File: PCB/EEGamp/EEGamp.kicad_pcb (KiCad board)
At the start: 2 copper layers, 92.4 x 113.1 mm, 100 parts, among them J1 Conn_02x17, Q1 BC847, Q2 BC847, Q3 BC847, Q4 BC847, Q5 BC857, Q6 BC857, Q7 BC857, Q8 BC857, U1 TLC277, U2 AD620, U3 AD620, U4 TLC277, U5 TLC277, U6 TLC277

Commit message: Test points added
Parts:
- added TP1: CH2, TestPoint:TestPoint_2Pads_Pitch2.54mm_Drill0.8mm, F.Cu at (143.7, 127.5)
- added TP2: CH1, TestPoint:TestPoint_2Pads_Pitch2.54mm_Drill0.8mm, F.Cu at (144.3, 100.5)
- added TP3: R_LEG, TestPoint:TestPoint_Loop_D1.80mm_Drill1.0mm_Beaded, F.Cu at (144.1, 87.5)
- added TP4: DC Check CH2, TestPoint:TestPoint_Loop_D1.80mm_Drill1.0mm_Beaded, F.Cu at (90.6, 112.3)
- added TP5: DC Check CH1, TestPoint:TestPoint_Loop_D1.80mm_Drill1.0mm_Beaded, F.Cu at (98.1, 89.4)
- added TP6: CalGND, TestPoint:TestPoint_Loop_D1.80mm_Drill1.0mm_Beaded, F.Cu at (148.2, 39.7)
- added TP7: CalU, TestPoint:TestPoint_Loop_D1.80mm_Drill1.0mm_Beaded, F.Cu at (139.0, 41.7)
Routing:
- net /R_LEG: track 10.2 -> 30.4 mm, vias 0 -> 1
- net Net-(C15-Pad2): track 7.11 -> 23.2 mm, vias 0 -> 1
- net /CH2+: track 0.00 -> 10.8 mm
- net /CH2-: track 0.00 -> 10.6 mm
- net /CH1-: track 0.00 -> 10.6 mm
- net /CH1+: track 0.00 -> 10.5 mm
- net Net-(R32-Pad2): track 0.00 -> 5.15 mm
- net Net-(R33-Pad2): track 0.00 -> 4.97 mm

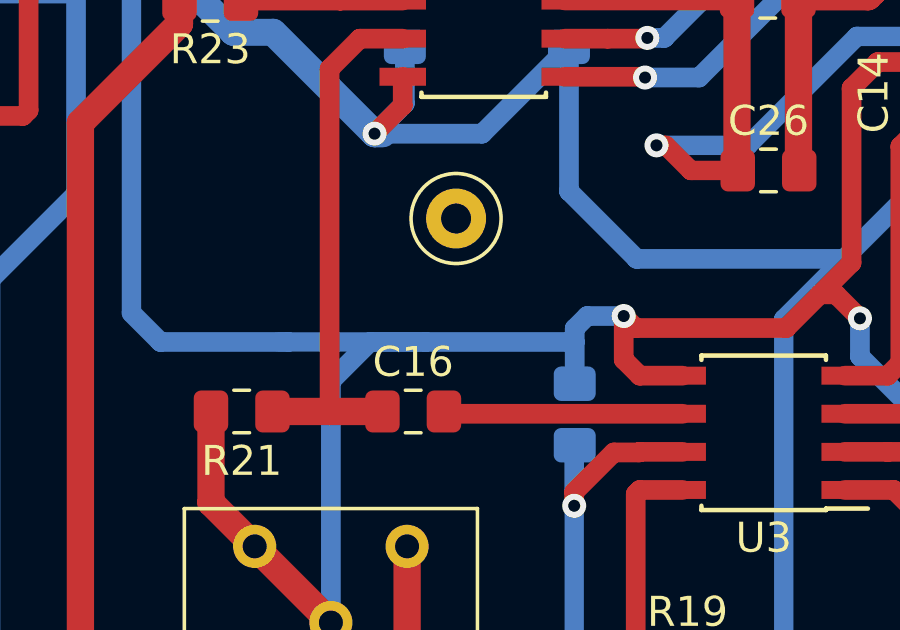
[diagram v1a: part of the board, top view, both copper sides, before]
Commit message: Fixed unrouted track
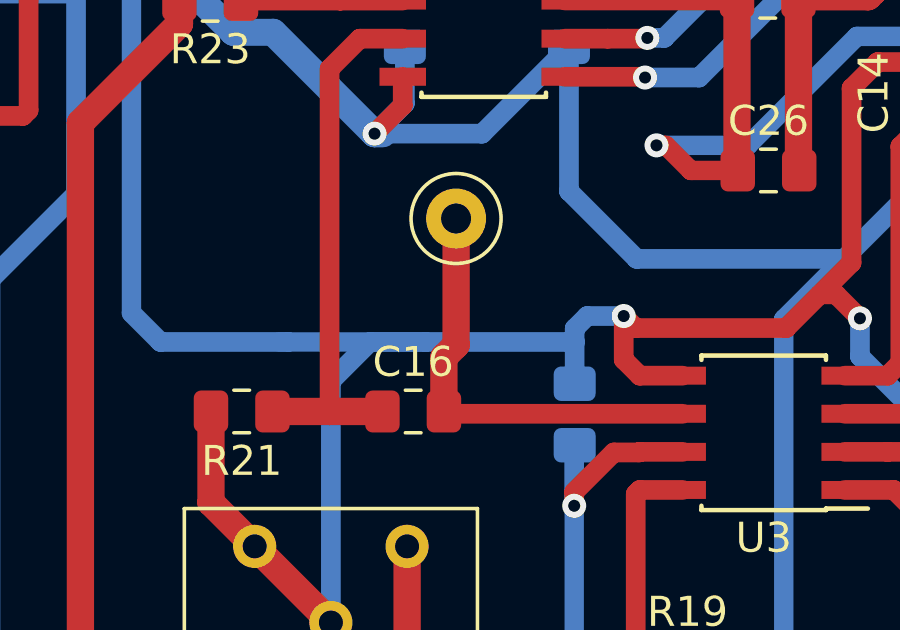
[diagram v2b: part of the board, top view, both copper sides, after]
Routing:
- net Net-(C16-Pad2): track 7.99 -> 14.6 mm
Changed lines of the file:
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@@
     (thickness 1.6)
     (drawings 8)
-    (tracks 924)
+    (tracks 927)
     (zones 0)
     (modules 107)
@@
   (segment (start 97.740308 95.865954) (end 97.664108 95.789754) (width 0.6564) (layer F.Cu) (net 16))
   (segment (start 105.623108 95.865954) (end 97.740308 95.865954) (width 0.6564) (layer F.Cu) (net 16))
+  (segment (start 97.664108 95.789754) (end 97.664108 93.978892) (width 0.9104) (layer F.Cu) (net 16))
+  (segment (start 98.0694 93.5736) (end 98.0694 89.3572) (width 0.9104) (layer F.Cu) (net 16))
+  (segment (start 97.664108 93.978892) (end 98.0694 93.5736) (width 0.9104) (layer F.Cu) (net 16))
   (segment (start 83.761143 127.349729) (end 83.676143 127.264729) (width 0.6564) (layer F.Cu) (net 17))
   (segment (start 83.761143 131.074729) (end 83.761143 127.349729) (width 0.6564) (layer F.Cu) (net 17))

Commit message: Project reborn! =]
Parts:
- removed C1, C2: 10pF, Capacitor_SMD:C_0805_2012Metric_Pad1.15x1.40mm_HandSolder
- removed C10, C11, C12, C13, C14, C27, C28, C30, C31, C32, C33, C9: 100nF, Capacitor_SMD:C_0805_2012Metric_Pad1.15x1.40mm_HandSolder
- removed C15, C16, C19, C20: 1μF, Capacitor_SMD:C_0805_2012Metric_Pad1.15x1.40mm_HandSolder
- removed C17, C18, C25, C26, C3, C4: 1nF, Capacitor_SMD:C_0805_2012Metric_Pad1.15x1.40mm_HandSolder
- removed C21, C22: 220nF 5%, Capacitor_SMD:C_0805_2012Metric_Pad1.15x1.40mm_HandSolder
- removed C23, C24: 33nF 5%, Capacitor_SMD:C_0805_2012Metric_Pad1.15x1.40mm_HandSolder
- removed C29: 47μF tan 1ohm, Capacitor_Tantalum_SMD:CP_EIA-2012-15_AVX-P_Pad1.30x1.05mm_HandSolder
- removed C34, C35: 10nF, Capacitor_SMD:C_0805_2012Metric_Pad1.15x1.40mm_HandSolder
- removed C36: 47μF, Capacitor_Tantalum_SMD:CP_EIA-2012-15_AVX-P_Pad1.30x1.05mm_HandSolder
- removed C5, C6, C7, C8: 100pF, Capacitor_SMD:C_0805_2012Metric_Pad1.15x1.40mm_HandSolder
- removed J1: Conn_02x17, Connector_IDC:IDC-Header_2x17_P2.54mm_Horizontal_Lock
- removed JP1, JP4: SJ201, Jumper:SolderJumper-2_P1.3mm_Open_RoundedPad1.0x1.5mm
- removed JP2, JP5: SJ202, Jumper:SolderJumper-2_P1.3mm_Open_RoundedPad1.0x1.5mm
- removed JP3, JP6: SJ203, Jumper:SolderJumper-2_P1.3mm_Open_RoundedPad1.0x1.5mm
- removed Q1, Q2, Q3, Q4: BC847, Package_TO_SOT_SMD:SOT-23
- removed Q5, Q6, Q7, Q8: BC857, Package_TO_SOT_SMD:SOT-23
- removed R1, R10, R11, R12, R13, R14, R16, R17, R18, R19, R2, R3, R4, R7, R8, R9: 2k2, Resistor_SMD:R_0805_2012Metric_Pad1.15x1.40mm_HandSolder
- removed R15, R28, R29, R32, R33, R6: 10k, Resistor_SMD:R_0805_2012Metric_Pad1.15x1.40mm_HandSolder
- removed R20, R21, R26, R27, R37, R40: 1M, Resistor_SMD:R_0805_2012Metric_Pad1.15x1.40mm_HandSolder
- removed R22, R23: 1k, Resistor_SMD:R_0805_2012Metric_Pad1.15x1.40mm_HandSolder
- removed R24, R25, R38, R39: 100k, Resistor_SMD:R_0805_2012Metric_Pad1.15x1.40mm_HandSolder
- removed R30, R31: 8.2k, Resistor_SMD:R_0805_2012Metric_Pad1.15x1.40mm_HandSolder
- removed R34, R35: 15k, Resistor_SMD:R_0805_2012Metric_Pad1.15x1.40mm_HandSolder
- removed R36: 100, Resistor_SMD:R_0805_2012Metric_Pad1.15x1.40mm_HandSolder
- removed R5: 200k, Resistor_SMD:R_0805_2012Metric_Pad1.15x1.40mm_HandSolder
- removed RV1, RV2, RV3: 20k, Potentiometer_THT:Potentiometer_Bourns_3296Y_Vertical
- removed TP1: CH2, TestPoint:TestPoint_2Pads_Pitch2.54mm_Drill0.8mm
- removed TP2: CH1, TestPoint:TestPoint_2Pads_Pitch2.54mm_Drill0.8mm
- removed TP3: R_LEG, TestPoint:TestPoint_Loop_D1.80mm_Drill1.0mm_Beaded
- removed TP4: DC Check CH2, TestPoint:TestPoint_Loop_D1.80mm_Drill1.0mm_Beaded
- removed TP5: DC Check CH1, TestPoint:TestPoint_Loop_D1.80mm_Drill1.0mm_Beaded
- removed TP6: CalGND, TestPoint:TestPoint_Loop_D1.80mm_Drill1.0mm_Beaded
- removed TP7: CalU, TestPoint:TestPoint_Loop_D1.80mm_Drill1.0mm_Beaded
- removed U1, U4, U5, U6: TLC277, Package_SO:SOIC-8_3.9x4.9mm_P1.27mm
- removed U2, U3: AD620, Package_SO:SOIC-8_3.9x4.9mm_P1.27mm
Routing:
- net /2.0V: track 484.1 -> 0.00 mm, vias 10 -> 0
- net GNDA: track 291.4 -> 0.00 mm, vias 6 -> 0
- net +5V: track 162.5 -> 0.00 mm, vias 7 -> 0
- net Net-(C34-Pad1): track 137.2 -> 0.00 mm, vias 5 -> 0
- net Net-(C27-Pad1): track 129.0 -> 0.00 mm, vias 2 -> 0
- net /ADIN1: track 124.9 -> 0.00 mm, vias 1 -> 0
- net /COM: track 115.2 -> 0.00 mm
- net Net-(R16-Pad2): track 99.1 -> 0.00 mm, vias 2 -> 0
- net /ADIN0: track 88.0 -> 0.00 mm, vias 2 -> 0
- net Net-(R18-Pad2): track 84.8 -> 0.00 mm, vias 2 -> 0
- net /PWM: track 70.1 -> 0.00 mm, vias 1 -> 0
- net Net-(C17-Pad2): track 69.6 -> 0.00 mm
- net Net-(R23-Pad2): track 47.0 -> 0.00 mm
- net Net-(C22-Pad1): track 37.4 -> 0.00 mm, vias 2 -> 0
- net Net-(C2-Pad2): track 35.8 -> 0.00 mm, vias 2 -> 0
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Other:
- board outline removed
